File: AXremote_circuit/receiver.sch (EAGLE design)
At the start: 0 parts

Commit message: Remote and receiver done.
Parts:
- added C1: 10uF, resistor:CPOL-EU153CLV-0405
- added C10, C4, C5: 100n, resistor:C-EUC0603
- added C11: 100nF, resistor:C-EUC0603K
- added C12, C18: 27pF, resistor:C-EUC0805K
- added C13: 39pF, resistor:C-EUC0805
- added C14, C15, C8: 2.7pF, resistor:C-EUC0805
- added C16: 3.6, resistor:C-EUC0805
- added C17: 6.2, resistor:C-EUC0805
- added C2: 0.01uF, resistor:C-EUC0805K
- added C3: 4.7u, resistor:C-EUC0805
- added C6, C7: 0, resistor:C-EUC0805
- added C9: 1uF, resistor:C-EUC0805K
- added D1, D2, D3: (no value), diode:DIODE-SOD123
- added D4: SFH482, led:SFH482
- added ERROR, ERROR_USB, PWR_LED: rot, led:LEDCHIPLED_1206
- added IC1: MEGA8-AI, atmel:MEGA8-AI
- added JP1: M02LOCK_LONGPADS, SparkFun-Connectors:M02LOCK_LONGPADS
- added L1, L2, L3, L4: 18nH, resistor:L-US0603
- added L5, L6: 12nH, resistor:L-US0603
- added LEARN_IR, LEARN_RF: gelb, led:LEDCHIPLED_1206
- added Q1: 16MHz, crystal:CRYSTALSM49
- added Q2: 12MHz, crystal:CRYSTALSM49
- added Q3: MOSFET-NCHANNELBSS138, SparkFun-DiscreteSemi:MOSFET-NCHANNELBSS138
- added R1, R10, R3, R5, R6, R7: 68, resistor:R-EU_R0603
- added R11, R12, R13, R4, R8, R9: 100, resistor:R-EU_R0603
- added R14: 10k, resistor:R-EU_R0603
- added R15: 1k5, resistor:R-EU_R0603
- added R16: 1M, resistor:R-EU_R0603
- added R2: 0, resistor:R-EU_R0603
- added RX_PACKET, RX_UART: grün, led:LEDCHIPLED_1206
- added S1: (no value), switch-omron:10-XX
- added U$1: LT1761, sam_eagle_parts:LT1761
- added U$2: AVR_SPI_PROG2PTH2, SparkFun-Connectors:AVR_SPI_PROG2PTH2
- added U$3: 2X5PIN-CONNECTOR, sam_eagle_parts:2X5PIN-CONNECTOR
- added U$4: POWER_JACK, sam_eagle_parts:POWER_JACK
- added U$5, U$6, U$7: IR LED, sam_eagle_parts:2PIN-CONNECTOR2.57RASTER
- added U$8: IR_RECEIVER, sam_eagle_parts:IR_RECEIVER
- added U$9: PC ATX Power En, sam_eagle_parts:2PIN-CONNECTOR2.57RASTER
- added U1: AX8052F143HS, axsem_v4-11:AX8052F143HS
- added X1: MINI-USB-SCHIELD-32005-201, con-cypressindustries:MINI-USB-SCHIELD-32005-201
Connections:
- new net D+: R1.2, R16.2, X1G$1.3
- new net D-: R15.1, R3.2, X1G$1.2
- new net DBG_CLK: U$3.5:DBG_CLK, U1IC.DBG_CLK/PB7
- new net DBG_DATA: U$3.6:DBG_DATA, U1IC.DBG_DATA/PB6
- new net DBG_EN: U$3.4:DBG_EN, U1IC.DBG_EN
- new net GND: C1.-, C10.2, C11.2, C12.1, C13.1, C16.1, C17.2, C18.2, C3.2, C4.1, C5.2, C6.1, C6.2, C7.1, C9.2, ERROR.C, ERROR_USB.C, IC1.GND, IC1.GND@1, IC1.GND@2, L3.2, L4.1, L6.2, LEARN_IR.C, LEARN_RF.C, PWR_LED.C, Q3.S, R14.1, R16.1, R2.1, RX_PACKET.C, RX_UART.C, U$1.GND, U$2.10, U$2.4, U$2.6, U$2.8, U$3.10:GND, U$3.2:GND, U$4.GND1, U$4.GND2, U$5.P$2, U$6.P$2, U$7.P$2, U$8.GND, U$9.P$2, U1GP.GND10, U1GP.GND11, U1GP.GND12, U1GP.GND13, U1GP.GND14, U1GP.GND15, U1GP.GND16, U1GP.GND17, U1GP.GND18, U1GP.GND19, U1GP.GND20, U1GP.GND21, U1GP.GND22, U1GP.GND23, U1GP.GND24, U1IC.GND1, U1IC.GND2, U1IC.GND3, U1IC.GND4, U1IC.TST1, U1IC.TST2, X1G$1.5, X1S.S1, X1S.S2, X1S.S3, X1S.S4
- new net N$1: U1IC.L1, U1IC.L2
- new net N$10: C14.1, L2.1
- new net N$11: C18.1, IC1.PB7(XTAL2/TOSC2), Q2.2
- new net N$12: C17.1, L1.2, L5.2
- new net N$13: C15.2, C16.2, L2.2, L6.1
- new net N$14: Q1.2, U1IC.CLK16P
- new net N$15: Q1.1, U1IC.CLK16N
- new net N$16: IC1.PD2(INT0), R1.1
- new net N$17: IC1.PD3(INT1), R3.1
- new net N$18: PWR_LED.A, R4.1
- new net N$19: IC1.PC6(/RESET), U$2.5
- new net N$2: C13.2, U1IC.FILT
- new net N$20: C15.1, C7.2, L5.1, R2.2
- new net N$21: IC1.PB4(MISO), U$2.9
- new net N$22: IC1.PB5(SCK), U$2.7
- new net N$23: IC1.PB3(MOSI/OC2), U$2.1
- new net N$24: D1.A, U$2.2
- new net N$25: R5.1, RX_PACKET.A
- new net N$26: R5.2, U1IC.PA5
- new net N$27: S1.P, S1.P1, U1IC.PA0
- new net N$28: LEARN_RF.A, R6.1
- new net N$29: LEARN_IR.A, R7.1
- new net N$3: C4.2, U1IC.VDDA1
- new net N$30: ERROR.A, R8.1
- new net N$31: R6.2, U1IC.PA4
- new net N$32: R7.2, U1IC.PA3
- new net N$33: R8.2, U1IC.PA2
- new net N$34: ERROR_USB.A, R9.1
- new net N$35: IC1.PD4(XCK/T0), R9.2
- new net N$36: R10.1, RX_UART.A
- new net N$38: D3.A, U$4.PIN
- new net N$39: R11.1, U1IC.PB2
- new net N$4: C2.2, U$1.BYP
- new net N$40: R12.1, U1IC.PB1
- new net N$41: R13.1, U1IC.PB0
- new net N$42: R13.2, U$7.P$1
- new net N$43: R12.2, U$6.P$1
- new net N$44: R11.2, U$5.P$1
- new net N$45: U$8.OUT, U1IC.PC1
- new net N$46: D4.A, R14.2, U1IC.PC0
- new net N$47: Q3.G, U1IC.PB3
- new net N$48: Q3.D, U$9.P$1
- new net N$49: D2.C, JP1.2
- new net N$5: C12.2, IC1.PB6(XTAL1/TOSC1), Q2.1
- new net N$50: IC1.PC5(ADC5/SCL), R10.2
- new net N$6: C5.1, U1IC.VDDA2
- new net N$7: C8.2, L4.2, U1IC.ANTP1
- new net N$8: C14.2, L3.1, U1IC.ANTN1
- new net N$9: C8.1, L1.1
- new net RST_N: U$3.3:!RST, U1IC.RST_N
- new net UART_AXIN: IC1.PD1(TXD), U1IC.PB5
- new net UART_AXOUT: IC1.PD0(RXD), U1IC.PB4
- new net VCC: C1.+, C10.1, C11.1, C2.1, C3.1, D4.C, IC1.AVCC, IC1.VCC@1, IC1.VCC@2, R15.2, R4.2, S1.S, S1.S1, U$1.OUT, U$3.1:VCC, U$8.VCC, U1IC.VDD_IO1, U1IC.VDD_IO2
- new net VCC_IN: C9.1, D1.C, D3.C, JP1.1, U$1.EN, U$1.IN
- new net VCC_USB: D2.A, X1G$1.1
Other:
- note added: "INPUT: 1.8 - 20V"
- note added: "IR PHOTOTRANSISTOR"
- note removed: "TODO: - USB 5V -> 3.3V Regulator - Status/Debug LED - IR LEDs (connectors?) - IR Receiver (1x with logic, 1x IR phototransistor) - Learn/Debug Button - AVR - AVR progheader - libv (usb)"
- note removed: "TODO: insert AX8052F143 here"

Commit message: Added a few keys.
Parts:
- added R17, R18: 100, resistor:R-EU_R0603
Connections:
- net GND: now also R18.1
- net N$27: now also R18.2
- net RST_N: now also R17.1
- net VCC: now also R17.2
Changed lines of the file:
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@@
 <?xml version="1.0" encoding="utf-8"?>
 <!DOCTYPE eagle SYSTEM "eagle.dtd">
-<eagle version="6.4">
+<eagle version="6.5.0">
 <drawing>
 <settings>
@@
 <part name="Q3" library="SparkFun-DiscreteSemi" deviceset="MOSFET-NCHANNEL" device="BSS138"/>
 <part name="JP1" library="SparkFun-Connectors" deviceset="M02" device="LOCK_LONGPADS"/>
+<part name="R17" library="resistor" deviceset="R-EU_" device="R0603" value="100"/>
+<part name="P+10" library="supply1" deviceset="VCC" device=""/>
+<part name="R18" library="resistor" deviceset="R-EU_" device="R0603" value="100"/>
+<part name="GND48" library="supply1" deviceset="GND" device=""/>
 </parts>
 <sheets>
@@
 <instance part="Q3" gate="G$1" x="63.5" y="-38.1" rot="R270"/>
 <instance part="JP1" gate="G$1" x="175.26" y="134.62" rot="R180"/>
+<instance part="R17" gate="G$1" x="50.8" y="12.7" rot="R180"/>
+<instance part="P+10" gate="VCC" x="40.64" y="12.7" rot="R90"/>
+<instance part="R18" gate="G$1" x="10.16" y="88.9" rot="R270"/>
+<instance part="GND48" gate="1" x="10.16" y="99.06" rot="R180"/>
 </instances>
 <busses>
@@
 <wire x1="58.42" y1="-38.1" x2="55.88" y2="-38.1" width="0.1524" layer="91"/>
 </segment>
+<segment>
+<pinref part="R18" gate="G$1" pin="1"/>
+<pinref part="GND48" gate="1" pin="GND"/>
+<wire x1="10.16" y1="96.52" x2="10.16" y2="93.98" width="0.1524" layer="91"/>
+</segment>
 </net>
 <net name="N$1" class="0">
@@
 <wire x1="152.4" y1="119.38" x2="152.4" y2="116.84" width="0.1524" layer="91"/>
 </segment>
+<segment>
+<pinref part="P+10" gate="VCC" pin="VCC"/>
+<pinref part="R17" gate="G$1" pin="2"/>
+<wire x1="43.18" y1="12.7" x2="45.72" y2="12.7" width="0.1524" layer="91"/>
+</segment>
 </net>
 <net name="N$2" class="0">
@@
 <wire x1="68.58" y1="0" x2="60.96" y2="0" width="0.1524" layer="91"/>
 <wire x1="60.96" y1="0" x2="60.96" y2="5.08" width="0.1524" layer="91"/>
+<pinref part="R17" gate="G$1" pin="1"/>
+<wire x1="55.88" y1="12.7" x2="60.96" y2="12.7" width="0.1524" layer="91"/>
+<wire x1="60.96" y1="12.7" x2="60.96" y2="5.08" width="0.1524" layer="91"/>
+<junction x="60.96" y="5.08"/>
 </segment>
 </net>
@@
 <pinref part="U1" gate="IC" pin="PA0"/>
 <junction x="10.16" y="73.66"/>
-</segment>
-</net>
+<pinref part="R18" gate="G$1" pin="2"/>
+<wire x1="10.16" y1="83.82" x2="10.16" y2="76.2" width="0.1524" layer="91"/>
+<junction x="10.16" y="76.2"/>
+</segment>
+</net>

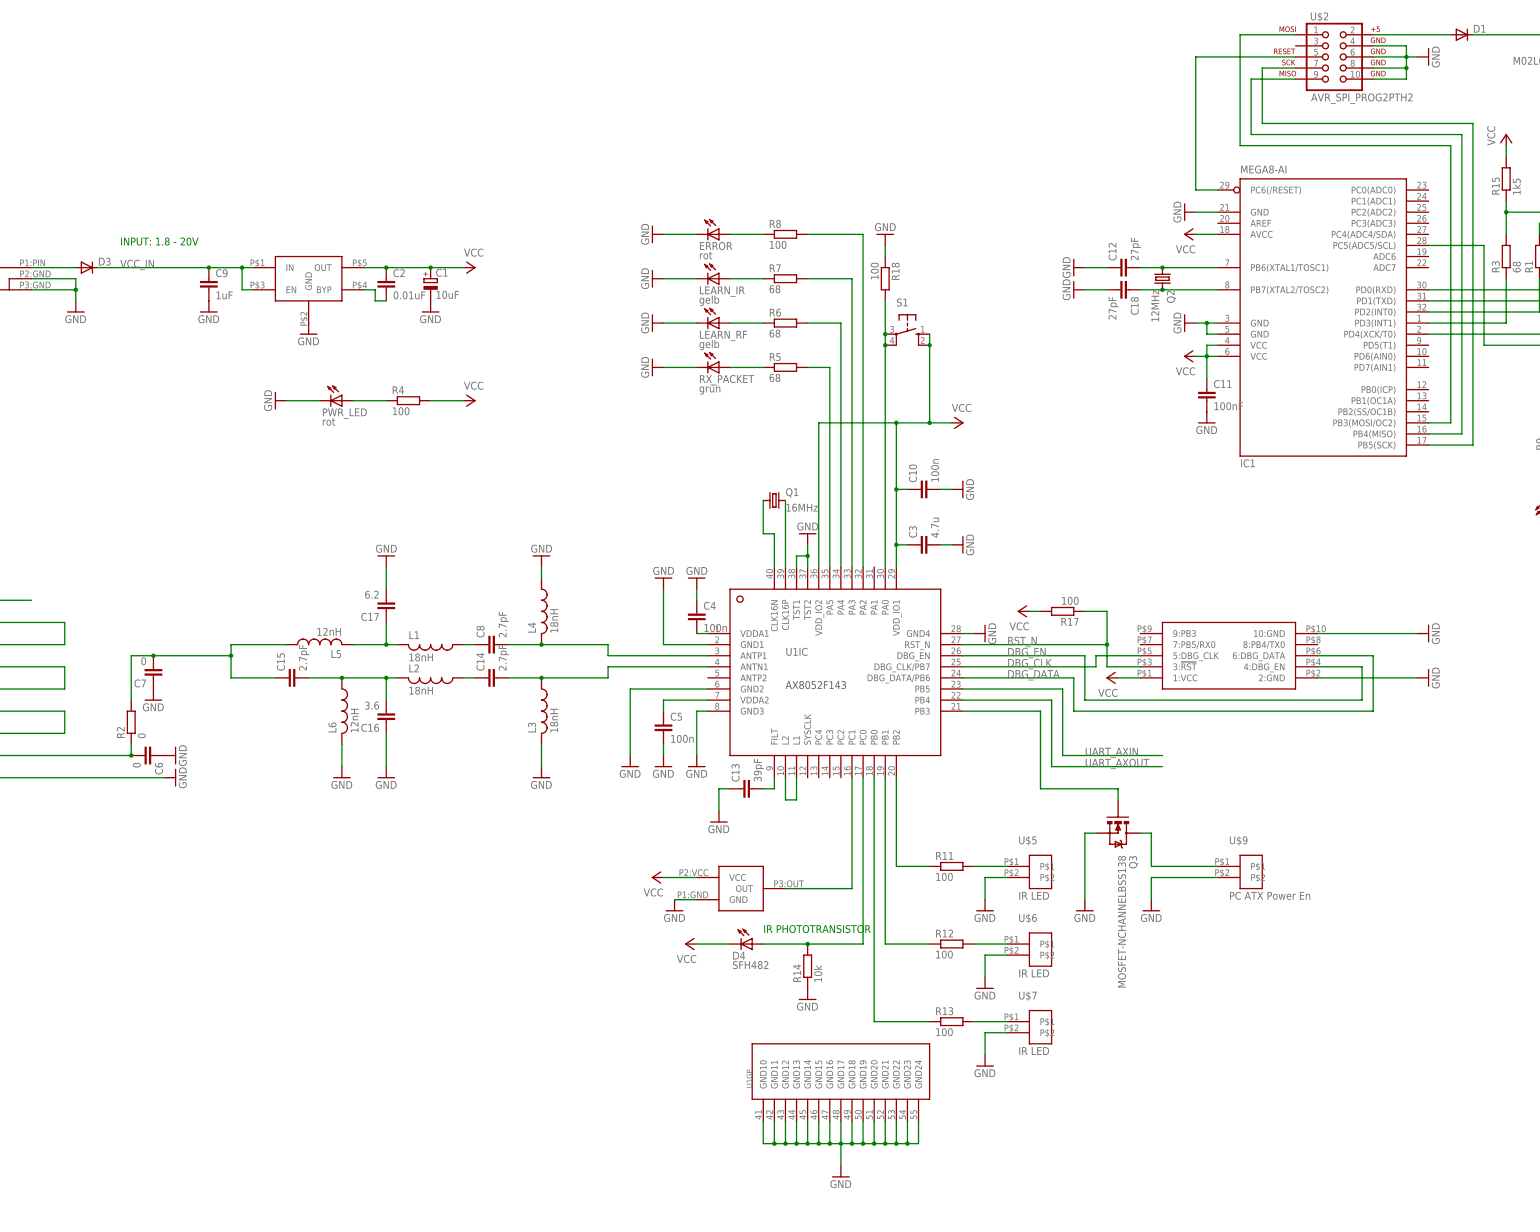
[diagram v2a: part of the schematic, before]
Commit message: Start work on receiver rev2.
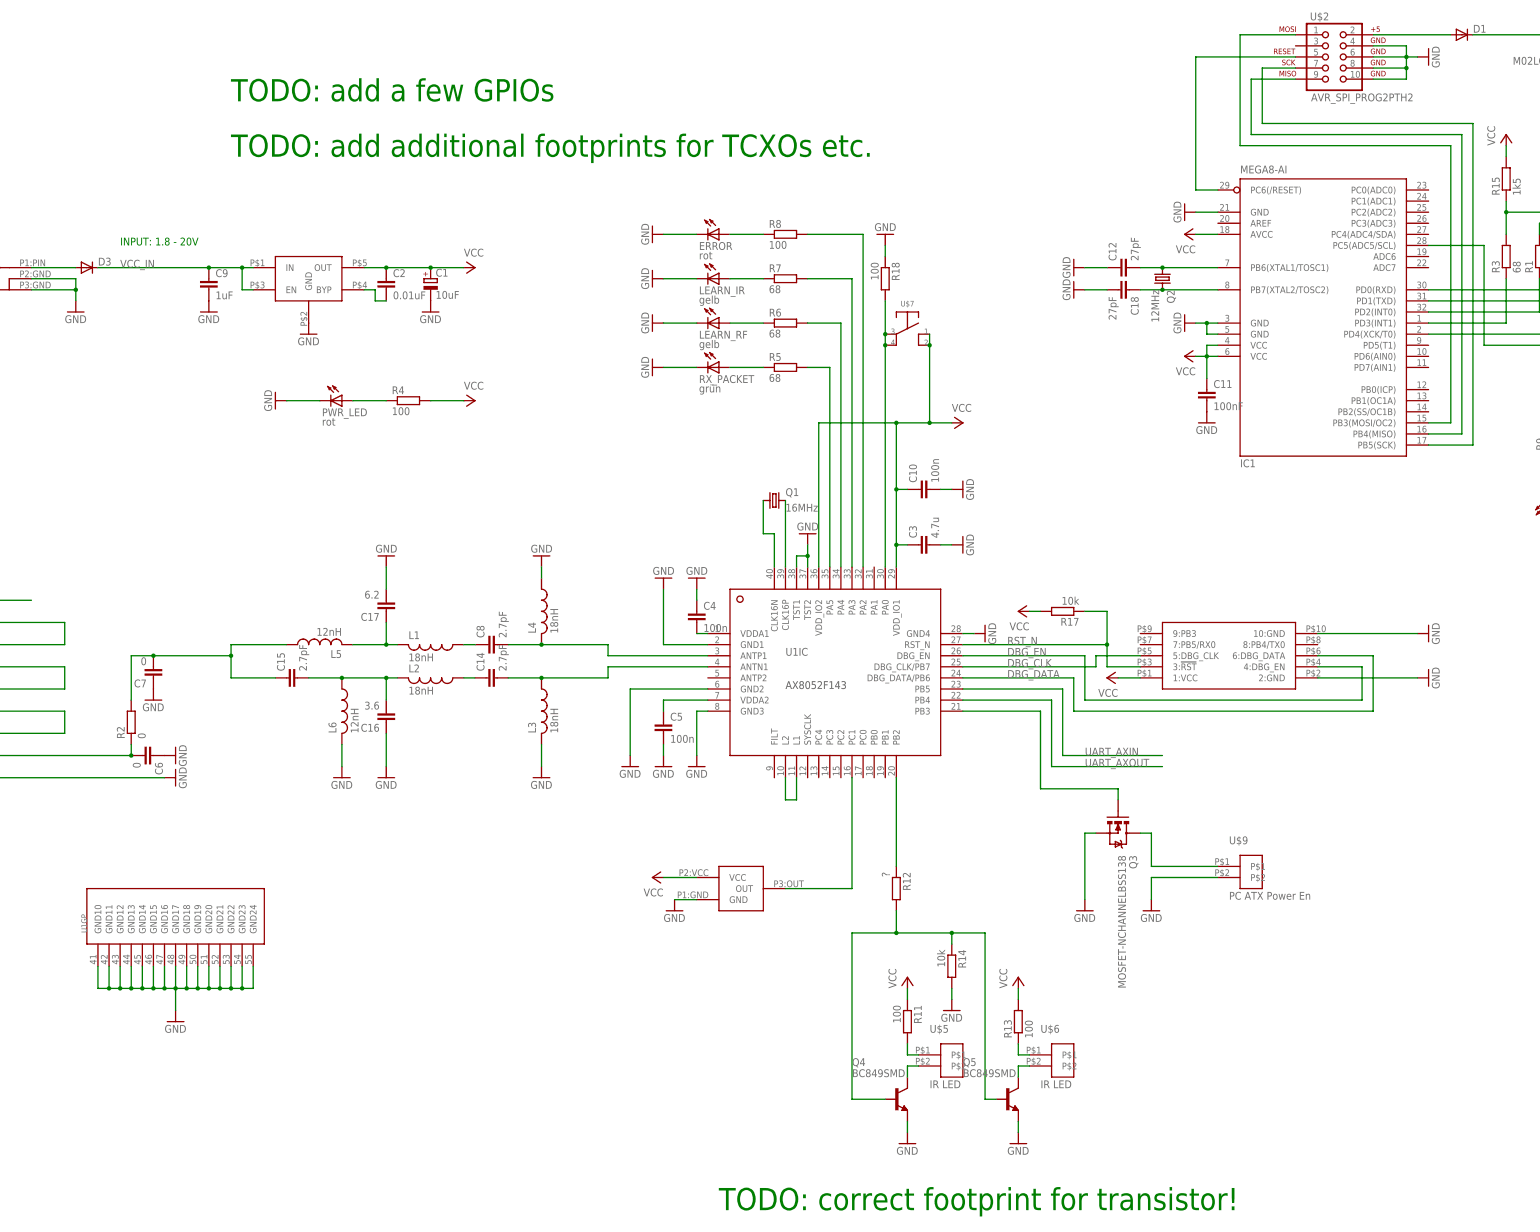
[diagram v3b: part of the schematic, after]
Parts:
- removed C13: 39pF, resistor:C-EUC0805
- removed D4: SFH482, led:SFH482
- removed S1: (no value), switch-omron:10-XX
- added Q4, Q5: BC849SMD, transistor-npn:BC849SMD
- C12, C18, C2: device resistor:C-EUC0805K -> resistor:C-EUC0603
- C14, C15, C16, C17, C6, C7, C8: device resistor:C-EUC0805 -> resistor:C-EUC0603
- R12: value 100 -> ?
- R17: value 100 -> 10k
- U$7: value IR LED -> SWITCHSMD; device sam_eagle_parts:2PIN-CONNECTOR2.57RASTER -> sam:SWITCHSMD
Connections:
- removed net N$2: C13.2, U1IC.FILT
- removed net N$46: D4.A, R14.2, U1IC.PC0
- net GND: now also Q4.E, Q5.E, R14.2; no longer C13.1, R14.1, U$5.P$2, U$6.P$2, U$7.P$2
- net N$27: now also U$7.P3, U$7.P4; no longer S1.P, S1.P1
- net N$39: now also Q4.C, U$5.P$2; no longer R11.1, U1IC.PB2
- net N$40: now also R13.1, U$6.P$1; no longer R12.1, U1IC.PB1
- net N$41: now also Q5.C, U$6.P$2; no longer R13.1, U1IC.PB0
- net N$42: now also R12.1, U1IC.PB2; no longer R13.2, U$7.P$1
- net N$43: now also Q4.B, Q5.B, R14.1; no longer U$6.P$1
- net VCC: now also R11.1, R13.2, U$7.P1, U$7.P2; no longer D4.C, S1.S, S1.S1
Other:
- note added: "TODO: add a few GPIOs"
- note added: "TODO: add additional footprints for TCXOs etc."
- note added: "TODO: correct footprint for transistor!"
- note removed: "IR PHOTOTRANSISTOR"
- moved on the sheet: R11, R12, R13, R14, U$5, U$6, U1GP

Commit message: Replace AVR with FT121 on receiver. Other details.
- Clean up schematics
- Use every pin of F143 (second button, GPIO)
- add TXCO and XTAL
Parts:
- removed D1, D2, D3: (no value), diode:DIODE-SOD123
- removed ERROR_USB: rot, led:LEDCHIPLED_1206
- removed IC1: MEGA8-AI, atmel:MEGA8-AI
- removed Q2: 12MHz, crystal:CRYSTALSM49
- removed Q4: BC849SMD, transistor-npn:BC849SMD
- removed RX_UART: grün, led:LEDCHIPLED_1206
- added BEAD: ferrite, resistor:R-EU_R0603
- added C13: 47pF, resistor:C-EUC0603K
- added C19: 100nF, resistor:C-EUC0603K
- added C20, C21: 100n, resistor:C-EUC0603
- added R19: 10k, resistor:R-EU_R0603
- added U$10: SWITCHSMD, sam:SWITCHSMD
- added X2: (no value), axsem_osc_v1-2:TCXO3225
- C12: value 27pF -> 47pF; device resistor:C-EUC0603 -> resistor:C-EUC0603K
- C18: value 27pF -> 10nF; device resistor:C-EUC0603 -> resistor:C-EUC0603K
- JP1: value M02LOCK_LONGPADS -> (none); device SparkFun-Connectors:M02LOCK_LONGPADS -> jumper:JP2E
- R1, R3: value 68 -> 27
- R10: value 68 -> 10k
- R15: value 1k5 -> 100
- R16: value 1M -> NC
- R9: value 100 -> 10k
- U$2: value AVR_SPI_PROG2PTH2 -> FT121; device SparkFun-Connectors:AVR_SPI_PROG2PTH2 -> sam:FT121
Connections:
- removed net N$23: IC1.PB3(MOSI/OC2), U$2.1
- removed net N$24: D1.A, U$2.2
- removed net N$34: ERROR_USB.A, R9.1
- removed net N$35: IC1.PD4(XCK/T0), R9.2
- removed net N$36: R10.1, RX_UART.A
- removed net N$38: D3.A, U$4.PIN
- removed net N$39: Q4.C, U$5.P$2
- removed net N$45: U$8.OUT, U1IC.PC1
- removed net N$49: D2.C, JP1.2
- removed net N$50: IC1.PC5(ADC5/SCL), R10.2
- removed net UART_AXIN: IC1.PD1(TXD), U1IC.PB5
- removed net UART_AXOUT: IC1.PD0(RXD), U1IC.PB4
- new net FTDI_!RESET: R9.2, U$2.!RESET, U1IC.PB0
- new net FTDI_SUSPEND: R10.2, U$2.SUSPEND, U1IC.PB1
- new net N$2: R1.1, U$2.DPLUS
- new net SPI_!INT: U$2.!INT, U1IC.PC4
- new net SPI_!SS: U$2.!SS, U1IC.PC0
- new net SPI_MISO: U$2.MISO, U1IC.PC3
- new net SPI_MOSI: U$2.MOSI, U1IC.PC2
- new net SPI_SCLK: U$2.SCLK, U1IC.PC1
- net D+: now also C13.1; no longer R16.2
- net D-: now also C12.1; no longer R15.1
- net GND: now also C12.2, C13.2, C18.1, C19.1, C20.2, JP1.3, R15.1, U$2.GND, X2.GND; no longer C12.1, C18.2, ERROR_USB.C, IC1.GND, IC1.GND@1, IC1.GND@2, Q4.E, RX_UART.C, U$2.10, U$2.4, U$2.6, U$2.8
- net N$11: now also BEAD.1, C11.1, U$2.VCC; no longer C18.1, IC1.PB7(XTAL2/TOSC2), Q2.2
- net N$14: now also R19.2
- net N$15: now also C21.1, R19.1
- net N$16: now also JP1.1, U1IC.PB4; no longer IC1.PD2(INT0), R1.1
- net N$17: now also R15.2, U$10.P3, U$10.P4, U1IC.PA1; no longer IC1.PD3(INT1), R3.1
- net N$19: now also R16.2, X2.VCONT; no longer IC1.PC6(/RESET), U$2.5
- net N$21: now also U$8.OUT, U1IC.PB3; no longer IC1.PB4(MISO), U$2.9
- net N$22: now also C21.2, X2.CLK; no longer IC1.PB5(SCK), U$2.7
- net N$41: now also U$5.P$2
- net N$43: no longer Q4.B
- net N$47: now also U1IC.PB5; no longer U1IC.PB3
- net N$5: now also R3.1, U$2.DMINUS; no longer C12.2, IC1.PB6(XTAL1/TOSC1), Q2.1
- net VCC: now also C19.2, C20.1, JP1.2, R10.1, R9.1, U$10.P1, U$10.P2, U$2.VBUS_S, U$2.VCC-IO, U$2.VOUT-3V3, X2.VDD; no longer C11.1, IC1.AVCC, IC1.VCC@1, IC1.VCC@2, R15.2
- net VCC_IN: now also U$4.PIN; no longer D1.C, D3.C, JP1.1
- net VCC_USB: now also BEAD.2, C18.2; no longer D2.A
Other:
- note added: "GPIO"
- note added: "INFRARED"
- note added: "POWER"
- note added: "PROGRAMMING"
- note added: "RF"
- note added: "SPI"
- note added: "USB"
- note added: "USER IO"
- note added: "optional TCXO instead of XTAL"
- note added: "rx"
- note added: "tx"
- note removed: "TODO: add a few GPIOs"
- note removed: "TODO: add additional footprints for TCXOs etc."
- moved on the sheet: C1, C11, C12, C18, C2, C9, ERROR, LEARN_IR, LEARN_RF, PWR_LED, Q1, Q3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
